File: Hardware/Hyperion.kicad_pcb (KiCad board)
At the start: 4 copper layers, 90.2 x 95.9 mm, 73 parts, among them J1 USB, J2 CONN-DC, Q1 MOSFET-P, Q2 FDC6561, U1 FT2232H, U2 93LC46/OT, U3 LTC4361-T, U4 TM4C123GH6PGE, U5 SN65HVD233, X1 12MHz, X2 12MHz, X3 32.768kHz

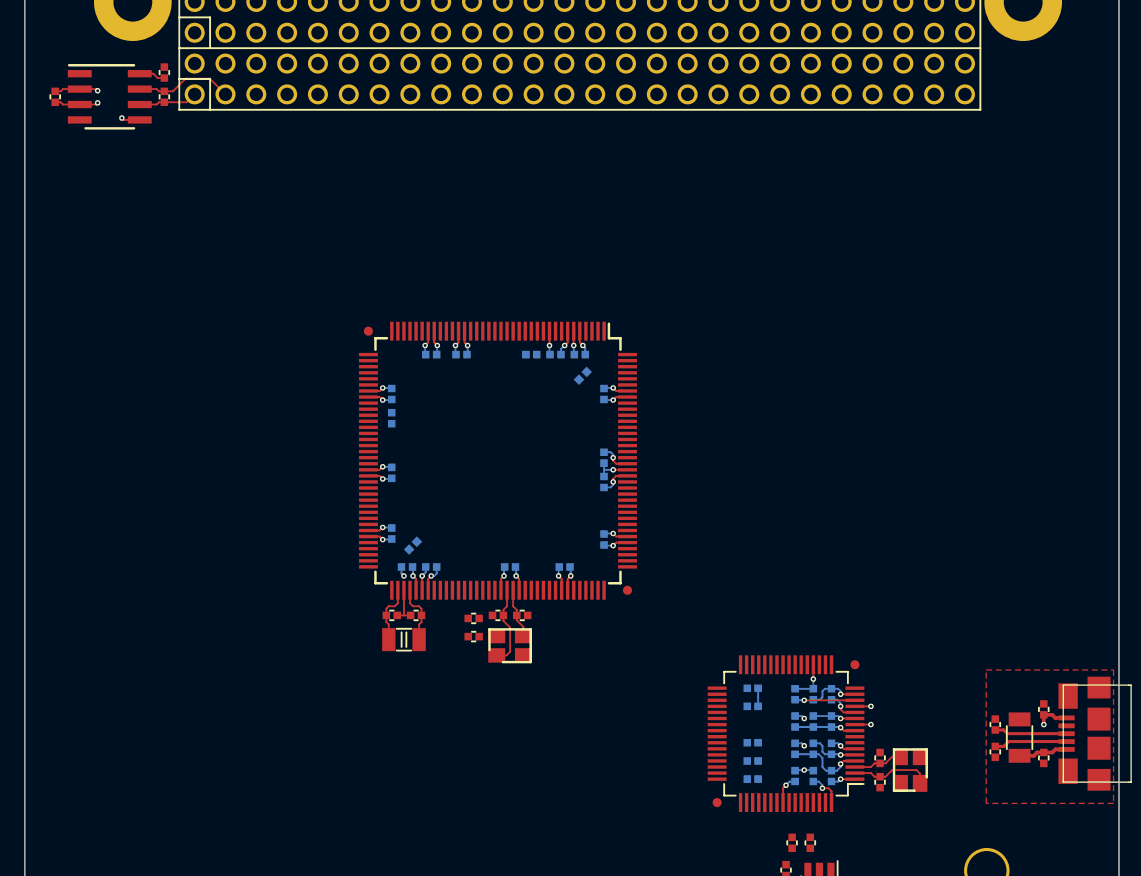
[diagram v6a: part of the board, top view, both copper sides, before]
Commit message: Switch to STM32F4 MCU
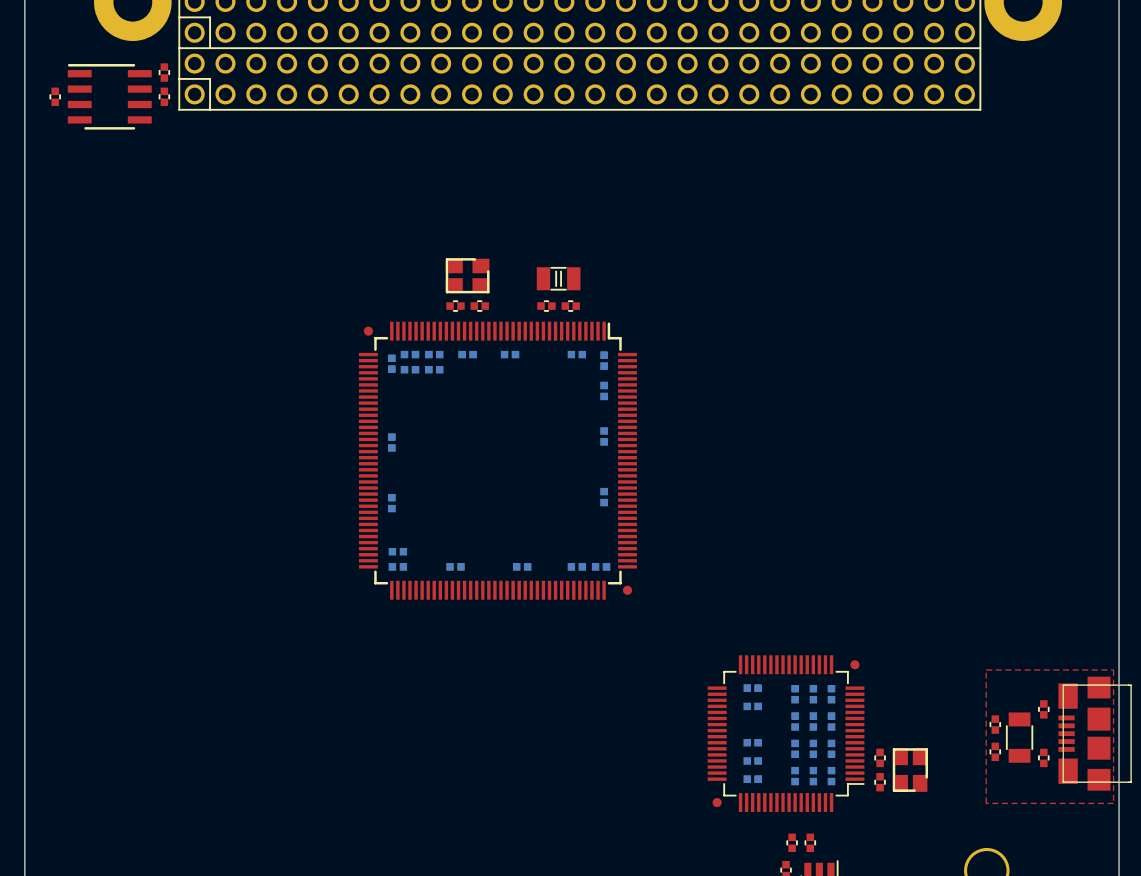
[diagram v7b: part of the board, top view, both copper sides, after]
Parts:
- removed C39: 0.1uF, CAPC1005-N
- C17, C18: value 0.1uF -> 2.2uF
- C29, C30: value 3.3uF -> 0.1uF
- R12: value 1k -> 10k; moved to B.Cu
- U4: value TM4C123GH6PGE -> STM32F407ZE
- moved X3 32.4 mm to (144.0, 77.0), turned to 180 degrees
- moved X2 30.7 mm to (136.5, 76.8), turned to 180 degrees
- moved C34 29.5 mm to (145.0, 79.2)
- moved C36 27.7 mm to (143.0, 79.2)
- moved C35 26.1 mm to (135.5, 79.2), turned to 180 degrees
- moved C33 25.5 mm to (137.5, 79.2), turned to 0 degrees
- moved C38 23.5 mm to (147.8, 83.8), turned to 270 degrees
- moved R12 22.9 mm to (147.8, 86.2), turned to 270 degrees
- moved C24 19.4 mm to (130.2, 84.0), turned to 90 degrees
- moved C28 18.8 mm to (135.5, 100.8), turned to 180 degrees
- moved C31 18.7 mm to (147.8, 95.0), turned to 270 degrees
- moved C27 18.4 mm to (130.8, 100.8), turned to 0 degrees
- moved C26 17.8 mm to (130.2, 95.5)
- moved C22 17.7 mm to (140.0, 83.2), turned to 0 degrees
- moved C32 17.6 mm to (131.8, 84.5), turned to 0 degrees
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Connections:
- C17 pad 1: +3.3V -> N-00000163
- C18 pad 1: +3.3V -> N-00000162
- C19 pad 1: +3.3V -> VMEM
- C20 pad 1: +3.3V -> /Core/RST
- C21 pad 1: +3.3V -> N-00000179
- C22 pad 1: +3.3V -> (no net)
- C22 pad 2: GND -> (no net)
- C23 pad 1: +3.3V -> (no net)
- C23 pad 2: GND -> (no net)
- C24 pad 1: +3.3V -> (no net)
- C24 pad 2: GND -> (no net)
- C25 pad 1: +3.3V -> (no net)
- C25 pad 2: GND -> (no net)
- C26 pad 1: +3.3V -> (no net)
- C26 pad 2: GND -> (no net)
- C27 pad 1: +3.3V -> (no net)
- C27 pad 2: GND -> (no net)
- C28 pad 1: +3.3V -> (no net)
- C28 pad 2: GND -> (no net)
- C29 pad 1: +3.3V -> (no net)
- C29 pad 2: GND -> (no net)
- C30 pad 1: +3.3V -> (no net)
- C30 pad 2: GND -> (no net)
- C31 pad 1: N-00000206 -> (no net)
- C31 pad 2: GND -> (no net)
- C32 pad 1: N-00000206 -> N-00000179
- C34 pad 2: /Core/GNDX -> (no net)
- C36 pad 2: /Core/GNDX -> (no net)
- C37 pad 1: N-00000115 -> (no net)
- C37 pad 2: GND -> (no net)
- C38 pad 1: VMEM -> (no net)
- C38 pad 2: GND -> (no net)
- FB3 pad 1: N-00000115 -> N-00000179
- H1 pad 2.17: /Core/ADCS0 -> (no net)
- H1 pad 2.18: /Core/ADCS1 -> (no net)
- H1 pad 2.19: /Core/ADCS2 -> (no net)
- H1 pad 2.20: /Core/ADCS3 -> (no net)
- H1 pad 2.21: /Core/ADCS4 -> (no net)
- H1 pad 2.22: /Core/ADCS5 -> (no net)
- H1 pad 2.23: /Core/ADCS6 -> (no net)
- H1 pad 2.24: /Core/ADCS7 -> (no net)
- R12 pad 1: /Core/RST -> GND
- R12 pad 2: +3.3V -> N-00000161
- U4 pad 10: GND -> (no net)
- U4 pad 101: +3.3V -> (no net)
- U4 pad 102: GND -> (no net)
- U4 pad 105: (no net) -> /Core/TMS
- U4 pad 106: (no net) -> N-00000163
- U4 pad 107: (no net) -> GND
- U4 pad 108: (no net) -> +3.3V
- U4 pad 109: (no net) -> /Core/TCK
- U4 pad 110: (no net) -> /Core/TDI
- U4 pad 113: +3.3V -> (no net)
- U4 pad 114: GND -> (no net)
- U4 pad 115: /Core/TDO -> (no net)
- U4 pad 116: /Core/TDI -> (no net)
- U4 pad 117: /Core/TMS -> (no net)
- U4 pad 118: /Core/TCK -> (no net)
- U4 pad 120: (no net) -> GND
- U4 pad 121: (no net) -> +3.3V
- U4 pad 124: +3.3V -> (no net)
- U4 pad 125: GND -> (no net)
- U4 pad 126: N-00000206 -> (no net)
- U4 pad 130: (no net) -> GND
- U4 pad 131: (no net) -> +3.3V
- U4 pad 133: (no net) -> /Core/TDO
- U4 pad 137: +3.3V -> (no net)
- U4 pad 138: GND -> N-00000161
- U4 pad 144: (no net) -> +3.3V
- U4 pad 16: (no net) -> GND
- U4 pad 17: (no net) -> +3.3V
- U4 pad 21: /Core/ADCS7 -> (no net)
- U4 pad 22: /Core/ADCS6 -> (no net)
- U4 pad 23: /Core/ADCS5 -> /Core/OSC0
- U4 pad 24: +3.3V -> /Core/OSC1
- U4 pad 25: GND -> /Core/RST
- U4 pad 26: /Core/ADCS4 -> (no net)
- U4 pad 27: /Core/ADCS3 -> (no net)
- U4 pad 28: /Core/ADCS2 -> (no net)
- U4 pad 29: +3.3V -> (no net)
- U4 pad 30: GND -> +3.3V
- U4 pad 31: /Core/ADCS1 -> GND
- U4 pad 32: /Core/ADCS0 -> (no net)
- U4 pad 33: (no net) -> N-00000179
- U4 pad 38: (no net) -> GND
- U4 pad 39: (no net) -> +3.3V
- U4 pad 43: +3.3V -> (no net)
- U4 pad 44: GND -> (no net)
- U4 pad 49: N-00000206 -> (no net)
- U4 pad 5: +3.3V -> (no net)
- U4 pad 51: (no net) -> GND
- U4 pad 52: (no net) -> +3.3V
- U4 pad 56: +3.3V -> (no net)
- U4 pad 57: GND -> (no net)
- U4 pad 6: GND -> VMEM
- U4 pad 61: (no net) -> GND
- U4 pad 62: (no net) -> +3.3V
- U4 pad 66: +3.3V -> (no net)
- U4 pad 67: GND -> (no net)
- U4 pad 7: N-00000115 -> (no net)
- U4 pad 71: (no net) -> N-00000162
- U4 pad 72: (no net) -> +3.3V
- U4 pad 74: /Core/XOSC0 -> (no net)
- U4 pad 75: /Core/GNDX -> (no net)
- U4 pad 76: /Core/XOSC1 -> (no net)
- U4 pad 77: VMEM -> (no net)
- U4 pad 78: +3.3V -> (no net)
- U4 pad 79: GND -> (no net)
- U4 pad 8: (no net) -> /Core/XOSC0
- U4 pad 83: (no net) -> GND
- U4 pad 84: (no net) -> +3.3V
- U4 pad 9: (no net) -> /Core/XOSC1
- U4 pad 90: /Core/RST -> (no net)
- U4 pad 91: GND -> (no net)
- U4 pad 92: /Core/OSC0 -> (no net)
- U4 pad 93: /Core/OSC1 -> (no net)
- U4 pad 94: +3.3V -> GND
- U4 pad 95: (no net) -> +3.3V
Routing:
- net GND: track 56.3 -> 0.00 mm, vias 24 -> 0
- net +3.3V: track 36.5 -> 0.00 mm, vias 17 -> 0
- net /Core/CANH: track 8.12 -> 0.00 mm
- net /Core/OSC0: track 6.65 -> 0.00 mm
- net /Interface Port/OSCI: track 6.65 -> 0.00 mm
- net N-00000110: track 6.41 -> 0.00 mm, vias 1 -> 0
- net /Interface Port/D-: track 6.04 -> 0.00 mm
- net /Interface Port/D+: track 6.00 -> 0.00 mm
- net +1.8V: track 5.57 -> 0.00 mm, vias 2 -> 0
- net N-00000111: track 5.05 -> 0.00 mm, vias 1 -> 0
- net /Interface Port/Reset: track 4.95 -> 0.00 mm, vias 1 -> 0
- net /Core/CANL: track 4.87 -> 0.00 mm
- net /Core/XOSC1: track 4.84 -> 0.00 mm
- net /Core/XOSC0: track 4.84 -> 0.00 mm
- net /Core/OSC1: track 4.12 -> 0.00 mm
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- added copper zone on Inner2.Cu, net +3.3V

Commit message: Clear core in prep for new MCU
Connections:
- C22 pad 1: (no net) -> +3.3V
- C22 pad 2: (no net) -> GND
- C23 pad 1: (no net) -> +3.3V
- C23 pad 2: (no net) -> GND
- C24 pad 1: (no net) -> +3.3V
- C24 pad 2: (no net) -> GND
- C25 pad 1: (no net) -> +3.3V
- C25 pad 2: (no net) -> GND
- C26 pad 1: (no net) -> +3.3V
- C26 pad 2: (no net) -> GND
- C27 pad 1: (no net) -> +3.3V
- C27 pad 2: (no net) -> GND
- C28 pad 1: (no net) -> +3.3V
- C28 pad 2: (no net) -> GND
- C29 pad 1: (no net) -> +3.3V
- C29 pad 2: (no net) -> GND
- C30 pad 1: (no net) -> +3.3V
- C30 pad 2: (no net) -> GND
- C31 pad 1: (no net) -> +3.3V
- C31 pad 2: (no net) -> GND
- C34 pad 2: (no net) -> GND
- C36 pad 2: (no net) -> GND
- C37 pad 1: (no net) -> +3.3V
- C37 pad 2: (no net) -> GND
- C38 pad 1: (no net) -> +3.3V
- C38 pad 2: (no net) -> GND
